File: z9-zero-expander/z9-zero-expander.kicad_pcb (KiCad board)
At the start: 2 copper layers, 29 x 58.4 mm, 3 parts, among them J1 Conn_DF40HC3.0-100DP-0.4V51, J2 Conn_01x50, J3 Conn_01x50

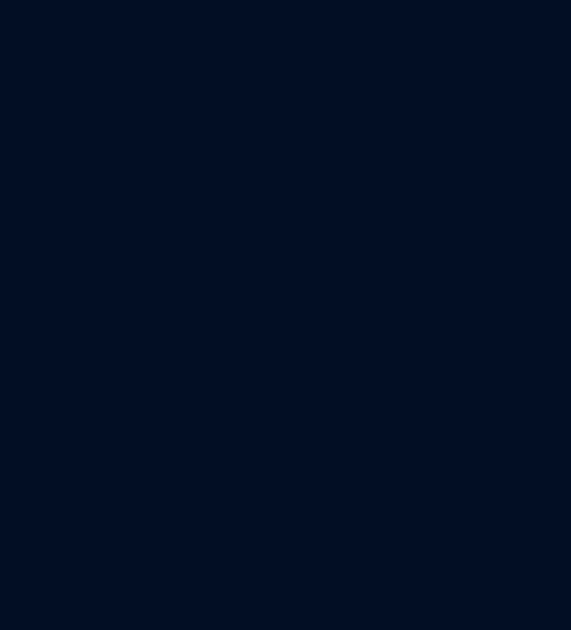
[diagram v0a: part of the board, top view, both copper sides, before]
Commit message: z9-zero-expander: migrate to KiCad 10 and add new sub-sheets
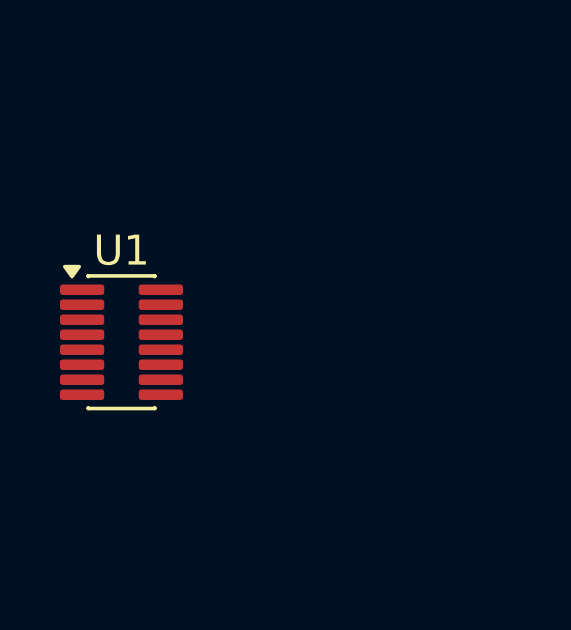
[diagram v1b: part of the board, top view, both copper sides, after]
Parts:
- added U1: TMUX1574DYY, Package_SO:Texas_DYY0016A_TSOT-23-16_2x4.2mm_P0.5mm, F.Cu at (123.2, 86.3)
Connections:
- J1 pad 1: Net-(J3-Pin_3) -> Net-(J3-Pin_1)
- J1 pad 10: unconnected-(J1-Pad10) -> Net-(J3-Pin_10)
- J1 pad 100: unconnected-(J1-Pad100) -> Net-(J2-Pin_50)
- J1 pad 11: Net-(J3-Pin_6) -> Net-(J3-Pin_11)
- J1 pad 12: unconnected-(J1-Pad12) -> Net-(J3-Pin_12)
- J1 pad 13: Net-(J3-Pin_7) -> Net-(J3-Pin_13)
- J1 pad 14: unconnected-(J1-Pad14) -> Net-(J3-Pin_14)
- J1 pad 15: Net-(J3-Pin_8) -> Net-(J3-Pin_15)
- J1 pad 16: unconnected-(J1-Pad16) -> Net-(J3-Pin_16)
- J1 pad 17: Net-(J3-Pin_10) -> Net-(J3-Pin_17)
- J1 pad 18: unconnected-(J1-Pad18) -> Net-(J3-Pin_18)
- J1 pad 19: unconnected-(J1-Pad19) -> Net-(J3-Pin_19)
- J1 pad 2: unconnected-(J1-Pad2) -> Net-(J3-Pin_2)
- J1 pad 20: unconnected-(J1-Pad20) -> Net-(J3-Pin_20)
- J1 pad 21: unconnected-(J1-Pad21) -> Net-(J3-Pin_21)
- J1 pad 22: unconnected-(J1-Pad22) -> Net-(J3-Pin_22)
- J1 pad 23: unconnected-(J1-Pad23) -> Net-(J3-Pin_23)
- J1 pad 24: unconnected-(J1-Pad24) -> Net-(J3-Pin_24)
- J1 pad 25: unconnected-(J1-Pad25) -> Net-(J3-Pin_25)
- J1 pad 26: unconnected-(J1-Pad26) -> Net-(J3-Pin_26)
- J1 pad 27: unconnected-(J1-Pad27) -> Net-(J3-Pin_27)
- J1 pad 28: unconnected-(J1-Pad28) -> Net-(J3-Pin_28)
- J1 pad 29: unconnected-(J1-Pad29) -> Net-(J3-Pin_29)
- J1 pad 3: Net-(J3-Pin_2) -> Net-(J3-Pin_3)
- J1 pad 30: unconnected-(J1-Pad30) -> Net-(J3-Pin_30)
- J1 pad 31: unconnected-(J1-Pad31) -> Net-(J3-Pin_31)
- J1 pad 32: unconnected-(J1-Pad32) -> Net-(J3-Pin_32)
- J1 pad 33: unconnected-(J1-Pad33) -> Net-(J3-Pin_33)
- J1 pad 34: unconnected-(J1-Pad34) -> Net-(J3-Pin_34)
- J1 pad 35: unconnected-(J1-Pad35) -> Net-(J3-Pin_35)
- J1 pad 36: unconnected-(J1-Pad36) -> Net-(J3-Pin_36)
- J1 pad 37: unconnected-(J1-Pad37) -> Net-(J3-Pin_37)
- J1 pad 38: unconnected-(J1-Pad38) -> Net-(J3-Pin_38)
- J1 pad 39: unconnected-(J1-Pad39) -> Net-(J3-Pin_39)
- J1 pad 4: unconnected-(J1-Pad4) -> Net-(J3-Pin_4)
- J1 pad 40: unconnected-(J1-Pad40) -> Net-(J3-Pin_40)
- J1 pad 41: unconnected-(J1-Pad41) -> Net-(J3-Pin_41)
- J1 pad 42: unconnected-(J1-Pad42) -> Net-(J3-Pin_42)
- J1 pad 43: unconnected-(J1-Pad43) -> Net-(J3-Pin_43)
- J1 pad 44: unconnected-(J1-Pad44) -> Net-(J3-Pin_44)
- J1 pad 45: unconnected-(J1-Pad45) -> Net-(J3-Pin_45)
- J1 pad 46: unconnected-(J1-Pad46) -> Net-(J3-Pin_46)
- J1 pad 47: unconnected-(J1-Pad47) -> Net-(J3-Pin_47)
- J1 pad 48: unconnected-(J1-Pad48) -> Net-(J3-Pin_48)
- J1 pad 49: unconnected-(J1-Pad49) -> Net-(J3-Pin_49)
- J1 pad 5: Net-(J3-Pin_3) -> Net-(J3-Pin_5)
- J1 pad 50: unconnected-(J1-Pad50) -> Net-(J3-Pin_50)
- J1 pad 51: unconnected-(J1-Pad51) -> Net-(J2-Pin_1)
- J1 pad 52: unconnected-(J1-Pad52) -> Net-(J2-Pin_2)
- J1 pad 53: unconnected-(J1-Pad53) -> Net-(J2-Pin_3)
- J1 pad 54: unconnected-(J1-Pad54) -> Net-(J2-Pin_4)
- J1 pad 55: unconnected-(J1-Pad55) -> Net-(J2-Pin_5)
- J1 pad 56: unconnected-(J1-Pad56) -> Net-(J2-Pin_6)
- J1 pad 57: unconnected-(J1-Pad57) -> Net-(J2-Pin_7)
- J1 pad 58: unconnected-(J1-Pad58) -> Net-(J2-Pin_8)
- J1 pad 59: unconnected-(J1-Pad59) -> Net-(J2-Pin_9)
- J1 pad 6: unconnected-(J1-Pad6) -> Net-(J3-Pin_6)
- J1 pad 60: unconnected-(J1-Pad60) -> Net-(J2-Pin_10)
- J1 pad 61: unconnected-(J1-Pad61) -> Net-(J2-Pin_11)
- J1 pad 62: unconnected-(J1-Pad62) -> Net-(J2-Pin_12)
- J1 pad 63: unconnected-(J1-Pad63) -> Net-(J2-Pin_13)
- J1 pad 64: unconnected-(J1-Pad64) -> Net-(J2-Pin_14)
- J1 pad 65: unconnected-(J1-Pad65) -> Net-(J2-Pin_15)
- J1 pad 66: unconnected-(J1-Pad66) -> Net-(J2-Pin_16)
- J1 pad 67: unconnected-(J1-Pad67) -> Net-(J2-Pin_17)
- J1 pad 68: unconnected-(J1-Pad68) -> Net-(J2-Pin_18)
- J1 pad 69: unconnected-(J1-Pad69) -> Net-(J2-Pin_19)
- J1 pad 7: Net-(J3-Pin_4) -> Net-(J3-Pin_7)
- J1 pad 70: unconnected-(J1-Pad70) -> Net-(J2-Pin_20)
- J1 pad 71: unconnected-(J1-Pad71) -> Net-(J2-Pin_21)
- J1 pad 72: unconnected-(J1-Pad72) -> Net-(J2-Pin_22)
- J1 pad 73: unconnected-(J1-Pad73) -> Net-(J2-Pin_23)
- J1 pad 74: unconnected-(J1-Pad74) -> Net-(J2-Pin_24)
- J1 pad 75: unconnected-(J1-Pad75) -> Net-(J2-Pin_25)
- J1 pad 76: unconnected-(J1-Pad76) -> Net-(J2-Pin_26)
- J1 pad 77: unconnected-(J1-Pad77) -> Net-(J2-Pin_27)
- J1 pad 78: unconnected-(J1-Pad78) -> Net-(J2-Pin_28)
- J1 pad 79: unconnected-(J1-Pad79) -> Net-(J2-Pin_29)
- J1 pad 8: unconnected-(J1-Pad8) -> Net-(J3-Pin_8)
- J1 pad 80: unconnected-(J1-Pad80) -> Net-(J2-Pin_30)
- J1 pad 81: unconnected-(J1-Pad81) -> Net-(J2-Pin_31)
- J1 pad 82: unconnected-(J1-Pad82) -> Net-(J2-Pin_32)
- J1 pad 83: unconnected-(J1-Pad83) -> Net-(J2-Pin_33)
- J1 pad 84: unconnected-(J1-Pad84) -> Net-(J2-Pin_34)
- J1 pad 85: unconnected-(J1-Pad85) -> Net-(J2-Pin_35)
- J1 pad 86: unconnected-(J1-Pad86) -> Net-(J2-Pin_36)
- J1 pad 87: unconnected-(J1-Pad87) -> Net-(J2-Pin_37)
- J1 pad 88: unconnected-(J1-Pad88) -> Net-(J2-Pin_38)
- J1 pad 89: unconnected-(J1-Pad89) -> Net-(J2-Pin_39)
- J1 pad 9: Net-(J3-Pin_5) -> Net-(J3-Pin_9)
- J1 pad 90: unconnected-(J1-Pad90) -> Net-(J2-Pin_40)
- J1 pad 91: unconnected-(J1-Pad91) -> Net-(J2-Pin_41)
- J1 pad 92: unconnected-(J1-Pad92) -> Net-(J2-Pin_42)
- J1 pad 93: unconnected-(J1-Pad93) -> Net-(J2-Pin_43)
- J1 pad 94: unconnected-(J1-Pad94) -> Net-(J2-Pin_44)
- J1 pad 95: unconnected-(J1-Pad95) -> Net-(J2-Pin_45)
- J1 pad 96: unconnected-(J1-Pad96) -> Net-(J2-Pin_46)
- J1 pad 97: unconnected-(J1-Pad97) -> Net-(J2-Pin_47)
- J1 pad 98: unconnected-(J1-Pad98) -> Net-(J2-Pin_48)
- J1 pad 99: unconnected-(J1-Pad99) -> Net-(J2-Pin_49)
- J2 pad 1: unconnected-(J2-Pin_1-Pad1) -> Net-(J2-Pin_1)
- J2 pad 10: unconnected-(J2-Pin_10-Pad10) -> Net-(J2-Pin_10)
- J2 pad 11: unconnected-(J2-Pin_11-Pad11) -> Net-(J2-Pin_11)
- J2 pad 12: unconnected-(J2-Pin_12-Pad12) -> Net-(J2-Pin_12)
- J2 pad 13: unconnected-(J2-Pin_13-Pad13) -> Net-(J2-Pin_13)
- J2 pad 14: unconnected-(J2-Pin_14-Pad14) -> Net-(J2-Pin_14)
- J2 pad 15: unconnected-(J2-Pin_15-Pad15) -> Net-(J2-Pin_15)
- J2 pad 16: unconnected-(J2-Pin_16-Pad16) -> Net-(J2-Pin_16)
- J2 pad 17: unconnected-(J2-Pin_17-Pad17) -> Net-(J2-Pin_17)
- J2 pad 18: unconnected-(J2-Pin_18-Pad18) -> Net-(J2-Pin_18)
- J2 pad 19: unconnected-(J2-Pin_19-Pad19) -> Net-(J2-Pin_19)
- J2 pad 2: unconnected-(J2-Pin_2-Pad2) -> Net-(J2-Pin_2)
- J2 pad 20: unconnected-(J2-Pin_20-Pad20) -> Net-(J2-Pin_20)
- J2 pad 21: unconnected-(J2-Pin_21-Pad21) -> Net-(J2-Pin_21)
- J2 pad 22: unconnected-(J2-Pin_22-Pad22) -> Net-(J2-Pin_22)
- J2 pad 23: unconnected-(J2-Pin_23-Pad23) -> Net-(J2-Pin_23)
- J2 pad 24: unconnected-(J2-Pin_24-Pad24) -> Net-(J2-Pin_24)
- J2 pad 25: unconnected-(J2-Pin_25-Pad25) -> Net-(J2-Pin_25)
- J2 pad 26: unconnected-(J2-Pin_26-Pad26) -> Net-(J2-Pin_26)
- J2 pad 27: unconnected-(J2-Pin_27-Pad27) -> Net-(J2-Pin_27)
- J2 pad 28: unconnected-(J2-Pin_28-Pad28) -> Net-(J2-Pin_28)
- J2 pad 29: unconnected-(J2-Pin_29-Pad29) -> Net-(J2-Pin_29)
- J2 pad 3: unconnected-(J2-Pin_3-Pad3) -> Net-(J2-Pin_3)
- J2 pad 30: unconnected-(J2-Pin_30-Pad30) -> Net-(J2-Pin_30)
- J2 pad 31: unconnected-(J2-Pin_31-Pad31) -> Net-(J2-Pin_31)
- J2 pad 32: unconnected-(J2-Pin_32-Pad32) -> Net-(J2-Pin_32)
- J2 pad 33: unconnected-(J2-Pin_33-Pad33) -> Net-(J2-Pin_33)
- J2 pad 34: unconnected-(J2-Pin_34-Pad34) -> Net-(J2-Pin_34)
- J2 pad 35: unconnected-(J2-Pin_35-Pad35) -> Net-(J2-Pin_35)
- J2 pad 36: unconnected-(J2-Pin_36-Pad36) -> Net-(J2-Pin_36)
- J2 pad 37: unconnected-(J2-Pin_37-Pad37) -> Net-(J2-Pin_37)
- J2 pad 38: unconnected-(J2-Pin_38-Pad38) -> Net-(J2-Pin_38)
- J2 pad 39: unconnected-(J2-Pin_39-Pad39) -> Net-(J2-Pin_39)
- J2 pad 4: unconnected-(J2-Pin_4-Pad4) -> Net-(J2-Pin_4)
- J2 pad 40: unconnected-(J2-Pin_40-Pad40) -> Net-(J2-Pin_40)
- J2 pad 41: unconnected-(J2-Pin_41-Pad41) -> Net-(J2-Pin_41)
- J2 pad 42: unconnected-(J2-Pin_42-Pad42) -> Net-(J2-Pin_42)
- J2 pad 43: unconnected-(J2-Pin_43-Pad43) -> Net-(J2-Pin_43)
- J2 pad 44: unconnected-(J2-Pin_44-Pad44) -> Net-(J2-Pin_44)
- J2 pad 45: unconnected-(J2-Pin_45-Pad45) -> Net-(J2-Pin_45)
- J2 pad 46: unconnected-(J2-Pin_46-Pad46) -> Net-(J2-Pin_46)
- J2 pad 47: unconnected-(J2-Pin_47-Pad47) -> Net-(J2-Pin_47)
- J2 pad 48: unconnected-(J2-Pin_48-Pad48) -> Net-(J2-Pin_48)
- J2 pad 49: unconnected-(J2-Pin_49-Pad49) -> Net-(J2-Pin_49)
- J2 pad 5: unconnected-(J2-Pin_5-Pad5) -> Net-(J2-Pin_5)
- J2 pad 50: unconnected-(J2-Pin_50-Pad50) -> Net-(J2-Pin_50)
- J2 pad 6: unconnected-(J2-Pin_6-Pad6) -> Net-(J2-Pin_6)
- J2 pad 7: unconnected-(J2-Pin_7-Pad7) -> Net-(J2-Pin_7)
- J2 pad 8: unconnected-(J2-Pin_8-Pad8) -> Net-(J2-Pin_8)
- J2 pad 9: unconnected-(J2-Pin_9-Pad9) -> Net-(J2-Pin_9)
- J3 pad 11: unconnected-(J3-Pin_11-Pad11) -> Net-(J3-Pin_11)
- J3 pad 12: unconnected-(J3-Pin_12-Pad12) -> Net-(J3-Pin_12)
- J3 pad 13: unconnected-(J3-Pin_13-Pad13) -> Net-(J3-Pin_13)
- J3 pad 14: unconnected-(J3-Pin_14-Pad14) -> Net-(J3-Pin_14)
- J3 pad 15: unconnected-(J3-Pin_15-Pad15) -> Net-(J3-Pin_15)
- J3 pad 16: unconnected-(J3-Pin_16-Pad16) -> Net-(J3-Pin_16)
- J3 pad 17: unconnected-(J3-Pin_17-Pad17) -> Net-(J3-Pin_17)
- J3 pad 18: unconnected-(J3-Pin_18-Pad18) -> Net-(J3-Pin_18)
- J3 pad 19: unconnected-(J3-Pin_19-Pad19) -> Net-(J3-Pin_19)
- J3 pad 20: unconnected-(J3-Pin_20-Pad20) -> Net-(J3-Pin_20)
- J3 pad 21: unconnected-(J3-Pin_21-Pad21) -> Net-(J3-Pin_21)
- J3 pad 22: unconnected-(J3-Pin_22-Pad22) -> Net-(J3-Pin_22)
- J3 pad 23: unconnected-(J3-Pin_23-Pad23) -> Net-(J3-Pin_23)
- J3 pad 24: unconnected-(J3-Pin_24-Pad24) -> Net-(J3-Pin_24)
- J3 pad 25: unconnected-(J3-Pin_25-Pad25) -> Net-(J3-Pin_25)
- J3 pad 26: unconnected-(J3-Pin_26-Pad26) -> Net-(J3-Pin_26)
- J3 pad 27: unconnected-(J3-Pin_27-Pad27) -> Net-(J3-Pin_27)
- J3 pad 28: unconnected-(J3-Pin_28-Pad28) -> Net-(J3-Pin_28)
- J3 pad 29: unconnected-(J3-Pin_29-Pad29) -> Net-(J3-Pin_29)
- J3 pad 30: unconnected-(J3-Pin_30-Pad30) -> Net-(J3-Pin_30)
- J3 pad 31: unconnected-(J3-Pin_31-Pad31) -> Net-(J3-Pin_31)
- J3 pad 32: unconnected-(J3-Pin_32-Pad32) -> Net-(J3-Pin_32)
- J3 pad 33: unconnected-(J3-Pin_33-Pad33) -> Net-(J3-Pin_33)
- J3 pad 34: unconnected-(J3-Pin_34-Pad34) -> Net-(J3-Pin_34)
- J3 pad 35: unconnected-(J3-Pin_35-Pad35) -> Net-(J3-Pin_35)
- J3 pad 36: unconnected-(J3-Pin_36-Pad36) -> Net-(J3-Pin_36)
- J3 pad 37: unconnected-(J3-Pin_37-Pad37) -> Net-(J3-Pin_37)
- J3 pad 38: unconnected-(J3-Pin_38-Pad38) -> Net-(J3-Pin_38)
- J3 pad 39: unconnected-(J3-Pin_39-Pad39) -> Net-(J3-Pin_39)
- J3 pad 40: unconnected-(J3-Pin_40-Pad40) -> Net-(J3-Pin_40)
- J3 pad 41: unconnected-(J3-Pin_41-Pad41) -> Net-(J3-Pin_41)
- J3 pad 42: unconnected-(J3-Pin_42-Pad42) -> Net-(J3-Pin_42)
- J3 pad 43: unconnected-(J3-Pin_43-Pad43) -> Net-(J3-Pin_43)
- J3 pad 44: unconnected-(J3-Pin_44-Pad44) -> Net-(J3-Pin_44)
- J3 pad 45: unconnected-(J3-Pin_45-Pad45) -> Net-(J3-Pin_45)
- J3 pad 46: unconnected-(J3-Pin_46-Pad46) -> Net-(J3-Pin_46)
- J3 pad 47: unconnected-(J3-Pin_47-Pad47) -> Net-(J3-Pin_47)
- J3 pad 48: unconnected-(J3-Pin_48-Pad48) -> Net-(J3-Pin_48)
- J3 pad 49: unconnected-(J3-Pin_49-Pad49) -> Net-(J3-Pin_49)
- J3 pad 50: unconnected-(J3-Pin_50-Pad50) -> Net-(J3-Pin_50)
- J3 pad 9: unconnected-(J3-Pin_9-Pad9) -> Net-(J3-Pin_9)
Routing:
- net (no net): track 85.6 -> 877.1 mm, vias 7 -> 82
- net Net-(J3-Pin_10): track 0.00 -> 31.5 mm, vias 0 -> 2
- net unconnected-(J1-Pad90): track 31.1 -> 0.00 mm, vias 2 -> 0
- net unconnected-(J1-Pad8): track 22.4 -> 0.00 mm, vias 1 -> 0
- net Net-(J3-Pin_8): track 15.1 -> 37.6 mm, vias 1 -> 2
- net unconnected-(J3-Pin_49-Pad49): track 20.3 -> 0.00 mm, vias 1 -> 0
- net Net-(J3-Pin_49): track 0.00 -> 20.3 mm, vias 0 -> 1
- net unconnected-(J1-Pad4): track 20.0 -> 0.00 mm, vias 1 -> 0
- net Net-(J3-Pin_4): track 17.5 -> 37.5 mm, vias 1 -> 2
- net unconnected-(J1-Pad12): track 20.0 -> 0.00 mm, vias 1 -> 0
- net unconnected-(J1-Pad14): track 18.7 -> 0.00 mm, vias 1 -> 0
- net unconnected-(J3-Pin_11-Pad11): track 18.3 -> 0.00 mm, vias 1 -> 0
- net unconnected-(J1-Pad16): track 18.1 -> 0.00 mm, vias 1 -> 0
- net unconnected-(J1-Pad20): track 18.1 -> 0.00 mm, vias 1 -> 0
- net unconnected-(J1-Pad10): track 17.6 -> 0.00 mm, vias 1 -> 0
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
